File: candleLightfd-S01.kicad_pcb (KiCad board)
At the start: 2 copper layers, 37.7 x 20 mm, 45 parts, among them P1 CONN_01X02, P2 CONN_01X02, T101 Tab, T102 Tab, T103 Tab, T104 Tab, U1 STM32G0B1CBT, U2 MCP1754ST-3302E/MB, U3 TJA1051T3, U4 TJA1051T3, X1 629722000214_pasteInHole, X3 TC2030-NL, Y1 830055299

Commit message: clean up
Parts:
- removed C10, C11, C8, C9: 100n_0603_X7R_10%_50V_-40C..125C_Chip-Capacitor, Capacitors_SMD:C_0603
- removed NB2: LAYERSTACK_TB, mechanical:LAYERSTACK_TB
- removed NB3, NB4: Passermarke_1mm_1.8mmx1.8mm, mechanical:Passermarke_1mm_1.8mmx1.8mm
- removed P1: CONN_01X02, Connector_generic:Header_1x2_Pitch2.54mm
- removed R1, R2: 5k1_0603_100mW_1%_E24_Chip-Resistor, Resistors_SMD:R_0603
- removed T101, T102, T103, T104: Tab, kikit:Tab
- removed TP1, TP2, TP3: TP2.0mm, Connector_generic:TP2.0mm
- removed U3, U4: TJA1051T3, tssop:SOIC-8_3.90mmx4.90mm_Pitch1.27mm
- removed X1: 629722000214_pasteInHole, Socket_GCT:USB4105_pasteInHole
- removed X2: ~, d-sub:D-SUB-9_side
- added C12: 100n_0603_X7R_10%_50V_-40C..125C_Chip-Capacitor, Capacitor_SMD:C_0603_1608Metric, F.Cu at (157.0, 142.0)
- added C13: 100n_0603_X7R_10%_50V_-40C..125C_Chip-Capacitor, Capacitor_SMD:C_0603_1608Metric, F.Cu at (154.9, 113.3)
- added J1: CAN1, Connector_PinHeader_2.54mm:PinHeader_1x04_P2.54mm_Horizontal, F.Cu at (177.2, 120.7)
- added J2: CAN2, Connector_PinHeader_2.54mm:PinHeader_1x04_P2.54mm_Horizontal, F.Cu at (177.2, 132.1)
- added J3: USB_C_Receptacle_USB2.0_16P, Connector_USB:USB_C_Receptacle_GCT_USB4085, F.Cu at (107.7, 126.7)
- added R10: 5k1_0603_100mW_1%_E24_Chip-Resistor, Resistor_SMD:R_0603_1608Metric, B.Cu at (103.5, 128.4)
- added R9: 5k1_0603_100mW_1%_E24_Chip-Resistor, Resistor_SMD:R_0603_1608Metric, B.Cu at (103.5, 130.9)
- added SW1: Term1, Button_Switch_THT:SW_Slide_SPDT_Angled_CK_OS102011MA1Q, F.Cu at (171.6, 121.4)
- added SW2: Term2, Button_Switch_THT:SW_Slide_SPDT_Angled_CK_OS102011MA1Q, F.Cu at (167.4, 139.1)
- added U5: ISO1044BD, Package_SO:SOIC-8_3.9x4.9mm_P1.27mm, F.Cu at (170.8, 127.0)
- added U6: ISO1044BD, Package_SO:SOIC-8_3.9x4.9mm_P1.27mm, F.Cu at (170.8, 133.3)
- added U7: NXE1S0505MC, Converter_DCDC:Converter_DCDC_Murata_NXExSxxxxMC_SMD, B.Cu at (170.8, 130.2)
- C1, C2, C3: footprint Capacitors_SMD:C_0603 -> Capacitor_SMD:C_0603_1608Metric
- C4, C5: footprint Capacitors_SMD:C_0603 -> Capacitor_SMD:C_0603_1608Metric; moved to B.Cu
- C6, C7: footprint Capacitors_SMD:C_0805 -> Capacitor_SMD:C_0805_2012Metric
- D1, D2, D3: footprint LEDs_Kingbright:LED_Kingbright_0603 -> LED_SMD:LED_0603_1608Metric
- P2: footprint Connector_generic:Header_1x2_Pitch2.54mm -> Jumper:SolderJumper-2_P1.3mm_Open_RoundedPad1.0x1.5mm
- R3, R4, R5, R6: footprint Resistors_SMD:R_0603 -> Resistor_SMD:R_0603_1608Metric
- R7: value 120R_0805_125mW_1%_E24_Chip-Resistor -> 120; footprint Resistors_SMD:R_0805 -> Resistor_SMD:R_0603_1608Metric; moved to B.Cu
- R8: value 120R_0805_125mW_1%_E24_Chip-Resistor -> 120; footprint Resistors_SMD:R_0805 -> Resistor_SMD:R_0603_1608Metric
- TP4, TP5: footprint Connector_generic:TP1.0mm -> TestPoint:TestPoint_Pad_1.0x1.0mm
- U1: footprint QFP:LQFP-48_7mmx7mm_Pitch0.5mm -> Package_QFP:LQFP-48_7x7mm_P0.5mm
- U2: footprint TO_SMD:SOT-89 -> Package_TO_SOT_SMD:SOT-89-3
- Y1: value 830055299 -> 830108313809; footprint crystal:Crystal_4Pin_SMD_3.2mmx2.5mm -> Crystal:Crystal_SMD_3225-4Pin_3.2x2.5mm
- moved NB1 79.4 mm to (45.1, 94.6)
- moved R7 40.7 mm to (170.8, 123.2), turned to 180 degrees
- moved R8 40.5 mm to (170.6, 137.2), turned to 180 degrees
- moved TP4 27.3 mm to (93.5, 119.6)
- moved P2 27.1 mm to (88.9, 149.9)
- moved R6 27.1 mm to (93.3, 149.9)
- moved C3 25.2 mm to (99.6, 135.8), turned to 180 degrees
- moved U2 23.0 mm to (106.2, 120.9), turned to 90 degrees
- moved C6 21.6 mm to (102.6, 122.1), turned to 90 degrees
- moved TP5 18.2 mm to (92.5, 121.8)
- moved C7 15.1 mm to (109.8, 122.1)
- moved Y1 13.0 mm to (116.1, 137.4), turned to 180 degrees
- moved C1 12.3 mm to (113.2, 137.4), turned to -90 degrees
- moved C2 10.2 mm to (119.0, 137.4), turned to 90 degrees
- moved C4 8.45 mm to (113.8, 131.4), turned to 90 degrees
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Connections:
- R7 pad 2: /CAN1_L -> Net-(SW1-B)
- R8 pad 2: /CAN2_L -> Net-(SW2-B)
- U1 pad 19: /CAN Transiver/CAN2_RX -> /CAN Transceiver/CAN2_RX
- U1 pad 20: /CAN Transiver/CAN2_TX -> /CAN Transceiver/CAN2_TX
- U1 pad 21: /CAN Transiver/CAN2_S -> unconnected-(U1B-PB2-Pad21)
- U1 pad 37: /CAN Transiver/CAN1_S -> unconnected-(U1A-PA15-Pad37)
- U1 pad 38: /CAN Transiver/CAN1_RX -> /CAN Transceiver/CAN1_RX
- U1 pad 39: /CAN Transiver/CAN1_TX -> /CAN Transceiver/CAN1_TX
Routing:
- net +3V3: track 83.2 -> 19.5 mm, vias 3 -> 2
- net +5V: track 65.2 -> 15.8 mm, vias 4 -> 0
- net GND: track 54.9 -> 6.09 mm, vias 16 -> 1
- net GNDD: track 0.00 -> 31.1 mm
- net /CAN Transiver/CAN2_S: track 28.3 -> 0.00 mm, vias 1 -> 0
- net /CAN Transiver/CAN2_RX: track 27.4 -> 0.00 mm, vias 1 -> 0
- net /MCU/NRST: track 27.2 -> 0.00 mm, vias 2 -> 0
- net /CAN Transiver/CAN1_S: track 21.7 -> 0.00 mm
- net /CAN Transiver/CAN2_TX: track 21.7 -> 0.00 mm, vias 1 -> 0
- net /MCU/SWCLK: track 20.9 -> 0.00 mm
- net /MCU/SWDIO: track 15.7 -> 0.00 mm, vias 2 -> 0
- net +5VD: track 0.00 -> 14.6 mm, vias 0 -> 2
- net /CAN Transiver/CAN1_RX: track 12.9 -> 0.00 mm
- net /MCU/RX: track 12.7 -> 0.00 mm
- net /CAN2_H: track 17.7 -> 5.60 mm
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- added copper zone on F.Cu, net GND
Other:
- board size 37.7 x 20 mm -> 116.8 x 57.2 mm
- board text removed: "+3V3"
- board text removed: "0"
- board text removed: "0 mm"
- board text removed: "0.01 mm"
- board text removed: "0.02"
- board text removed: "0.035 mm"
- board text removed: "1"
- board text removed: "1.51 mm"
- board text removed: "12V"
- board text removed: "3.3"
- board text removed: "4.5"
- board text removed: "5V"
- board text removed: "B.Cu"
- board text removed: "B.Mask"
- board text removed: "B.Paste"
- board text removed: "B.Silkscreen"
- board text removed: "Black"
- board text removed: "Bottom Silk Screen"
- board text removed: "Bottom Solder Mask"
- board text removed: "Bottom Solder Paste"
- board text removed: "Color"
- board text removed: "Dielectric 1"
- board text removed: "Epsilon R"
- board text removed: "F.Cu"
- board text removed: "F.Mask"
- board text removed: "F.Paste"
- board text removed: "F.Silkscreen"
- board text removed: "FR4"
- board text removed: "GND"
- board text removed: "Layer Name"
- board text removed: "Loss Tangent"
- board text removed: "Material"
- board text removed: "Not specified"
- board text removed: "Thickness (mm)"
- board text removed: "Top Silk Screen"
- board text removed: "Top Solder Mask"
- board text removed: "Top Solder Paste"
- board text removed: "Type"
- board text removed: "White"
- board text removed: "copper"
- board text removed: "core"

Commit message: gsi-v1
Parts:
- removed C4: 100n, Capacitor_SMD:C_0603_1608Metric
- removed TP4, TP5: TP1.0mm, TestPoint:TestPoint_Pad_1.0x1.0mm
- removed U6: ISO1044BD, Package_SO:SOIC-8_3.9x4.9mm_P1.27mm
- removed U7: NXE1S0505MC, Converter_DCDC:Converter_DCDC_Murata_NXExSxxxxMC_SMD
- added C10: 10u_0603_X7R_10%_50V_-40C..125C_Chip-Capacitor, Capacitor_SMD:C_0603_1608Metric, B.Cu at (121.5, 129.3)
- added C11: 100n_0603_X7R_10%_50V_-40C..125C_Chip-Capacitor, Capacitor_SMD:C_0603_1608Metric, B.Cu at (121.5, 132.3)
- added C8: 10u_0603_X7R_10%_50V_-40C..125C_Chip-Capacitor, Capacitor_SMD:C_0603_1608Metric, B.Cu at (135.9, 129.6)
- added C9: 100n_0603_X7R_10%_50V_-40C..125C_Chip-Capacitor, Capacitor_SMD:C_0603_1608Metric, F.Cu at (132.9, 131.2)
- added U3: R05CTE05S, Package_SO:SOIC-16W_7.5x10.3mm_P1.27mm, B.Cu at (128.2, 129.6)
- added U4: ISO1044BD, Package_SO:SOIC-8_3.9x4.9mm_P1.27mm, F.Cu at (128.2, 132.4)
- C5: moved to F.Cu
- C7: value 10u_0805_X7R_10%_10V_-40C..125C_Chip-Capacitor -> 1u_0805_X7R_10%_10V_-40C..125C_Chip-Capacitor
- moved NB1 78.4 mm to (115.1, 129.8), turned to 0 degrees
- moved SW1 48.0 mm to (126.7, 138.3), turned to 0 degrees
- moved J2 42.7 mm to (136.3, 120.0)
- moved U5 42.6 mm to (128.2, 126.9)
- moved R8 42.4 mm to (130.4, 123.4)
- moved J1 42.4 mm to (136.3, 131.7)
- moved R7 42.3 mm to (130.4, 135.9)
- moved SW2 41.0 mm to (130.7, 121.0), turned to 180 degrees
- moved C12 38.3 mm to (123.0, 124.4), turned to 180 degrees
- moved C13 35.4 mm to (123.7, 129.9), turned to 90 degrees
- moved P2 25.7 mm to (111.7, 137.9), turned to 90 degrees
- moved C3 23.7 mm to (116.9, 119.6), turned to 0 degrees
- moved R6 23.7 mm to (113.8, 137.9), turned to -90 degrees
- moved C1 17.5 mm to (121.7, 122.1), turned to 90 degrees
- moved R3 15.9 mm to (117.7, 137.9), turned to 90 degrees
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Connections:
- R7 pad 2: Net-(SW1-B) -> Net-(SW1-C)
- R8 pad 2: Net-(SW2-B) -> Net-(SW2-A)
- SW1 pad 1: /CAN1_L -> unconnected-(SW1-A-Pad1)
- SW1 pad 2: Net-(SW1-B) -> /CAN1_L
- SW1 pad 3: unconnected-(SW1-C-Pad3) -> Net-(SW1-C)
- SW2 pad 1: /CAN2_L -> Net-(SW2-A)
- SW2 pad 2: Net-(SW2-B) -> /CAN2_L
- U1 pad 29: /MCU/TX -> unconnected-(U1A-PA9-Pad29)
- U1 pad 32: /MCU/RX -> unconnected-(U1A-PA10-Pad32)
- U5 pad 2: /CAN Transceiver/CAN1_TX -> /CAN Transceiver/CAN2_TX
- U5 pad 3: /CAN Transceiver/CAN1_RX -> /CAN Transceiver/CAN2_RX
- U5 pad 5: /CAN1_L -> /CAN2_L
- U5 pad 6: /CAN1_H -> /CAN2_H
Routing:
- net +3V3: track 19.5 -> 71.3 mm, vias 2 -> 3
- net GNDD: track 31.1 -> 3.64 mm, vias 0 -> 1
- net /MCU/NRST: track 0.00 -> 27.4 mm, vias 0 -> 2
- net +5V: track 15.8 -> 40.6 mm
- net /CAN Transceiver/CAN2_TX: track 0.00 -> 16.7 mm
- net /MCU/LED_RX: track 0.00 -> 16.6 mm, vias 0 -> 2
- net /CAN Transceiver/CAN2_RX: track 0.00 -> 16.5 mm, vias 0 -> 2
- net /MCU/SWCLK: track 0.00 -> 14.6 mm, vias 0 -> 2
- net /MCU/LED_TX: track 0.07 -> 13.5 mm, vias 0 -> 2
- net /CAN Transceiver/CAN1_RX: track 0.00 -> 10.9 mm
- net /CAN Transceiver/CAN1_TX: track 0.00 -> 10.8 mm
- net /CAN1_L: track 4.20 -> 13.7 mm
- net /MCU/SWDIO: track 0.00 -> 8.97 mm
- net +5VD: track 14.6 -> 23.5 mm, vias 2 -> 1
- net /USB_P: track 1.70 -> 10.5 mm
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- added copper zone on B.Cu, net GNDD
- added copper zone on F.Cu, net GNDD
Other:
- board size 116.8 x 57.2 mm -> 40 x 22.5 mm
- board text added: "CAN 1"
- board text added: "CAN 2"
- board text added: "GSI GmbH v 1.0 10/2024"
- board text added: "candlelightFD"
- board text added: "x G H L"
- board text removed: "${prefix}-P${type_number}-R${release}-B${pcb_variant}-C${pcb_ci}"

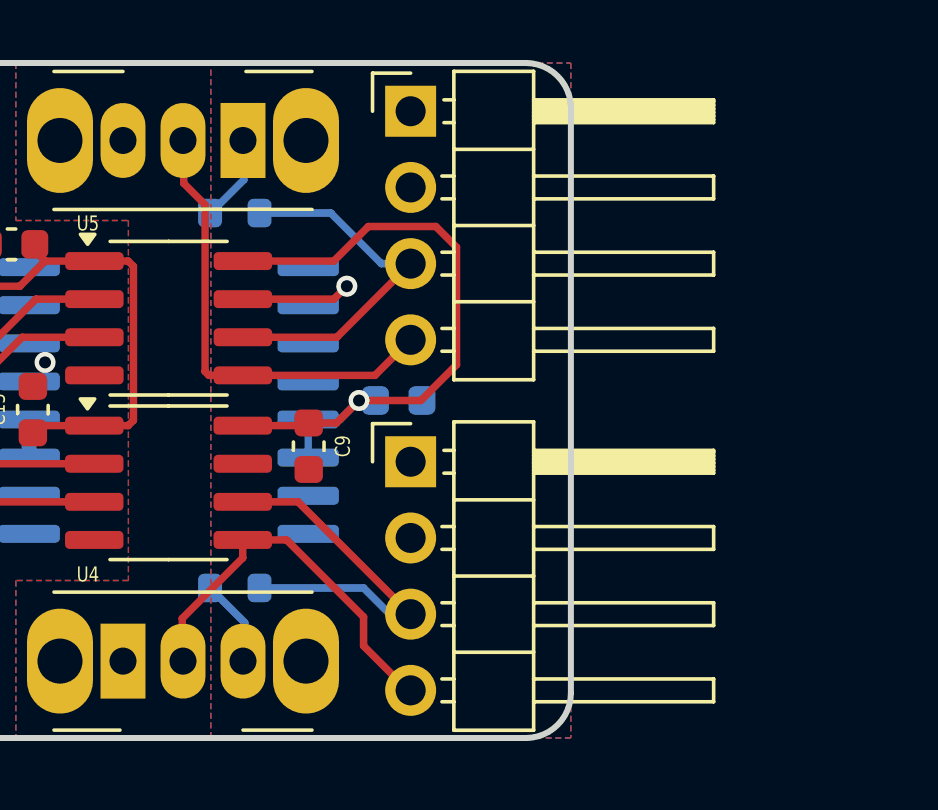
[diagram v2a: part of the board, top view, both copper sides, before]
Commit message: replace connector CAN1/2 with PSS
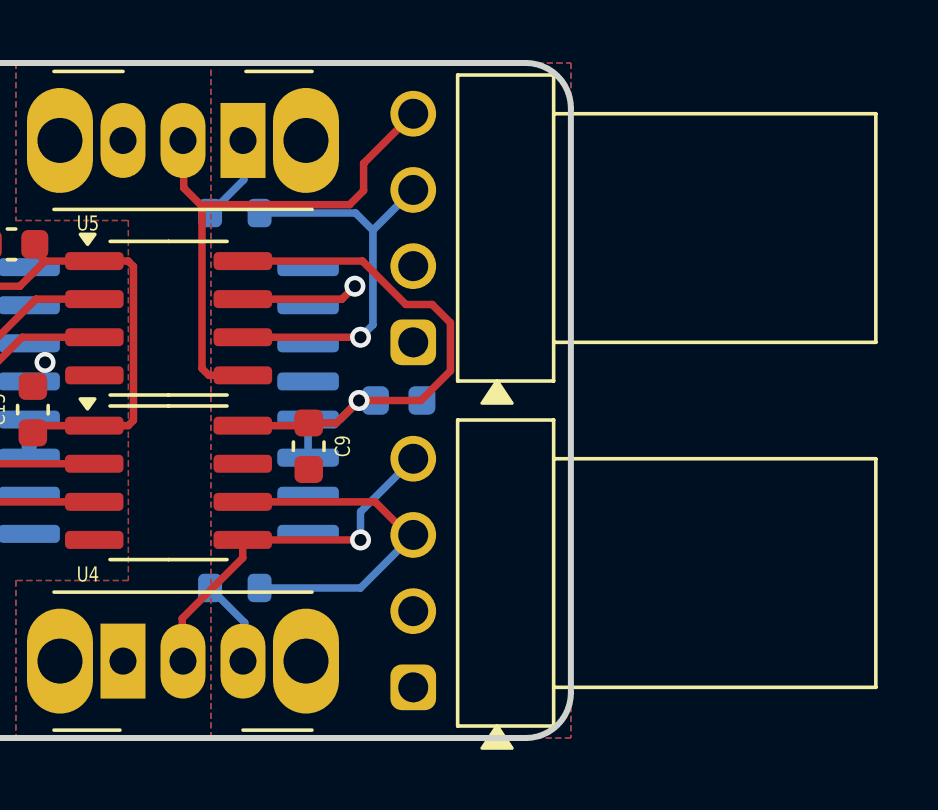
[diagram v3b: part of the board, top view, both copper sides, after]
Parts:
- J1, J2: footprint Connector_PinHeader_2.54mm:PinHeader_1x04_P2.54mm_Horizontal -> Connector_PSS254:PSS254_1x04_Horizontal
- moved J2 7.70 mm to (136.4, 127.7)
- moved J1 7.52 mm to (136.4, 139.2)
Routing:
- net /CAN2_L: track 15.5 -> 18.3 mm
- net +5VD: track 23.5 -> 20.8 mm
- net /CAN2_H: track 12.3 -> 13.6 mm, vias 0 -> 1
- net /CAN1_L: track 13.7 -> 12.6 mm, vias 0 -> 1
- net /CAN1_H: track 12.7 -> 11.8 mm
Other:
- board text added: "L H G x"
- board text removed: "x G H L"

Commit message: ready for production
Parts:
- C1, C2: value 6p2_0603_C0G_5%_50V_-40C..125C_Chip-Capacitor -> 6p2
- C10, C8: value 10u_0603_X7R_10%_50V_-40C..125C_Chip-Capacitor -> 10u
- C11, C12, C13, C9: value 100n_0603_X7R_10%_50V_-40C..125C_Chip-Capacitor -> 100n
- C6: value 10u_0805_X7R_10%_10V_-40C..125C_Chip-Capacitor -> 10u; footprint Capacitor_SMD:C_0805_2012Metric -> Capacitor_SMD:C_0603_1608Metric
- C7: value 1u_0805_X7R_10%_10V_-40C..125C_Chip-Capacitor -> 1u; footprint Capacitor_SMD:C_0805_2012Metric -> Capacitor_SMD:C_0603_1608Metric
- R10, R9: value 5k1_0603_100mW_1%_E24_Chip-Resistor -> 5k1
- R3, R4, R5: value 1k_0603_100mW_1%_E24_Chip-Resistor -> 1k
- R6: value 10k_0603_100mW_1%_E24_Chip-Resistor -> 10k
- moved C8 0.66 mm to (136.6, 129.6)
- moved D3 0.62 mm to (113.7, 121.4)
- moved R5 0.62 mm to (112.1, 121.4)
- moved C7 0.34 mm to (110.2, 122.4)
- moved C6 0.34 mm to (103.6, 122.4)
- moved NB1 0.21 mm to (115.3, 129.8)
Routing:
- net +5VD: track 20.8 -> 21.5 mm
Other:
- board text added: "JLCJLCJLCJLC"
